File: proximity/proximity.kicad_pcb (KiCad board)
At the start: 2 copper layers, 40 x 30 mm, 32 parts, among them IC1 NRF51822, P1 CONN_3X2, P2 ST-0503, P3 AIN_0_3, P4 AIN_4_7, Q1 MOSFET_N, SW1 SWITCH-4, SW2 SWITCH-4, U1 ANTENNA-NC, X1 FOX924

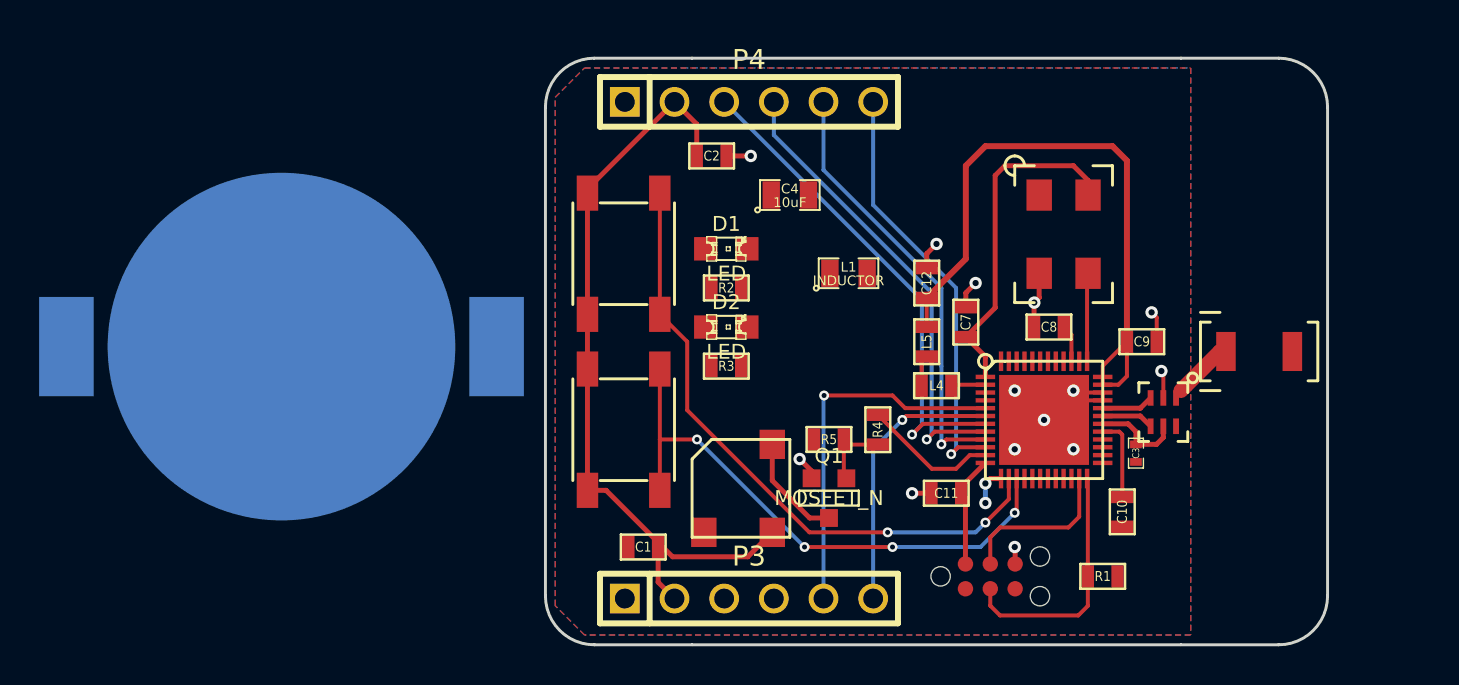
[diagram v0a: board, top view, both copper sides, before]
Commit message: Proximity tag routing done
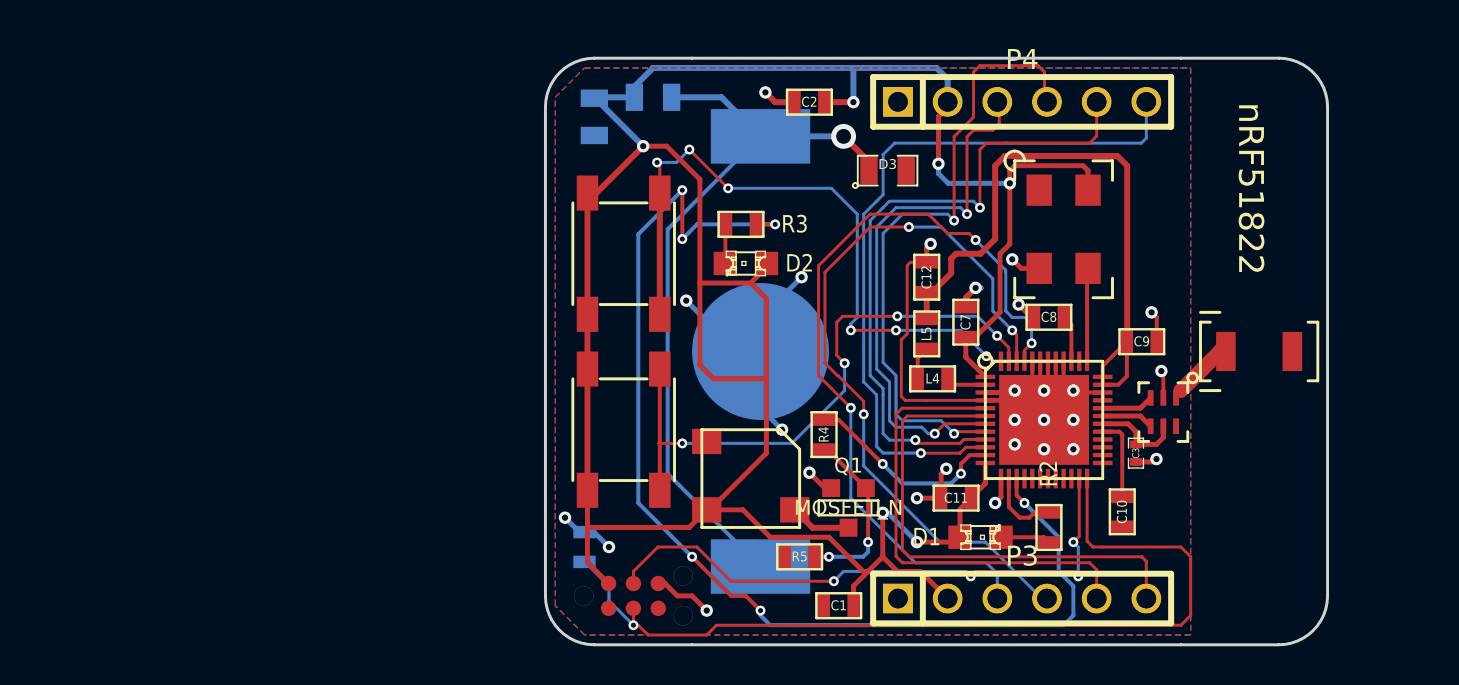
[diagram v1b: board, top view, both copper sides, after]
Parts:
- added D3: DIODE, SM0805, F.Cu at (112.5, 105.8)
- C4, L1, R1: moved to B.Cu
- moved R1 26.5 mm to (97.0, 125.0), turned to 90 degrees
- moved BT1 24.5 mm to (106.0, 115.0), turned to 90 degrees
- moved R2 20.6 mm to (120.8, 124.0), turned to 90 degrees
- moved D1 19.7 mm to (117.2, 124.5)
- moved P1 18.3 mm to (99.5, 127.5)
- moved P3 14.0 mm to (119.4, 127.6)
- moved P4 14.0 mm to (119.4, 102.2)
- moved L1 13.5 mm to (100.5, 102.0), turned to 180 degrees
- moved C4 10.8 mm to (97.5, 103.0), turned to 270 degrees
- moved C1 10.4 mm to (110.0, 128.0)
- moved R3 7.29 mm to (105.0, 108.5)
- moved R5 6.18 mm to (108.0, 125.5)
- moved C2 5.71 mm to (108.5, 102.2), turned to 0 degrees
- moved D2 3.40 mm to (105.2, 110.5), turned to 180 degrees
- moved R4 2.76 mm to (109.2, 119.2)
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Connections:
- IC1 pad 14: /SW1 -> /LED1
- IC1 pad 15: /SW2 -> /LED2
- IC1 pad 3: (no net) -> GND
- IC1 pad 4: (no net) -> GND
- IC1 pad 40: (no net) -> GND
- IC1 pad 41: (no net) -> GND
- IC1 pad 42: (no net) -> GND
- IC1 pad 43: (no net) -> GND
- IC1 pad 44: (no net) -> GND
- IC1 pad 47: (no net) -> /SW2
- IC1 pad 48: (no net) -> /SW1
- R2 pad 2: (no net) -> /LED1
- R3 pad 2: (no net) -> /LED2
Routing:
- net VCC: track 62.6 -> 145.2 mm, vias 0 -> 6
- net /LED2: track 0.00 -> 58.9 mm, vias 0 -> 6
- net GND: track 34.8 -> 86.4 mm, vias 16 -> 27
- net /AIN0: track 0.00 -> 40.5 mm, vias 0 -> 3
- net /AIN1: track 0.00 -> 38.3 mm, vias 0 -> 3
- net N-000003: track 0.00 -> 37.8 mm, vias 0 -> 1
- net /SWCLK: track 12.8 -> 46.1 mm, vias 0 -> 1
- net /SWDIO: track 8.30 -> 30.5 mm, vias 0 -> 4
- net /AIN7: track 21.8 -> 37.1 mm
- net /AIN6: track 22.4 -> 33.9 mm, vias 1 -> 2
- net /AIN3: track 14.1 -> 25.6 mm, vias 1 -> 0
- net /AIN5: track 23.9 -> 32.2 mm, vias 1 -> 2
- net N-0000029: track 3.88 -> 9.16 mm, vias 0 -> 2
- net /AIN2: track 18.9 -> 24.0 mm, vias 1 -> 0
- net /LED1: track 0.00 -> 3.84 mm
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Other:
- net class logic added: clearance 0.1524, trace_width 0.1524, via_dia 0.508, via_drill 0.381
- board text added: "Guan Yang 2013"
- board text added: "nRF51822"

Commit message: Minor changes
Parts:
- added D4: DIODE, SM0805, F.Cu at (107.8, 113.5)
- IC1: footprint QFN48+1-0.4MM -> QFN48+1-0.4MM-SHORTPADS
- moved R5 8.43 mm to (106.2, 117.2)
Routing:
- net N-0000024: track 3.13 -> 11.8 mm
- net GND: track 86.4 -> 94.2 mm, vias 27 -> 28
- net VCC: track 145.2 -> 139.0 mm
- net N-0000030: track 9.16 -> 9.74 mm
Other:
- board text added: "01A2"
- board text added: "02A3"
- board text added: "03A4"
- board text added: "04A5"
- board text added: "05A6"
- board text added: "06A7"
- board text added: "26A0"
- board text added: "27A1"
- board text added: "3V3"
- board text added: "GND"

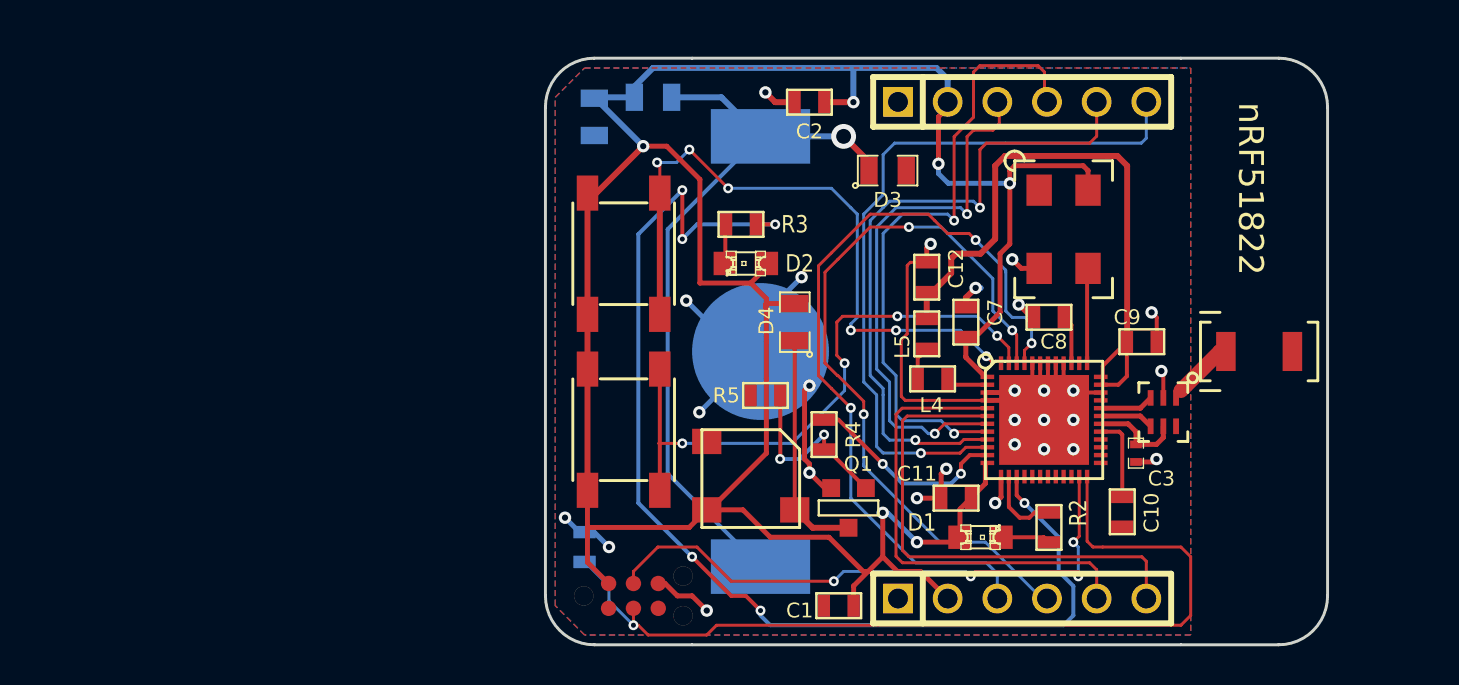
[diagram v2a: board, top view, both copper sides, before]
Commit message: nRF51822 proximity tag updates: - Ordinary crystal instead of CMOS oscillator - Regular pin header for SWDIO and SWCLK
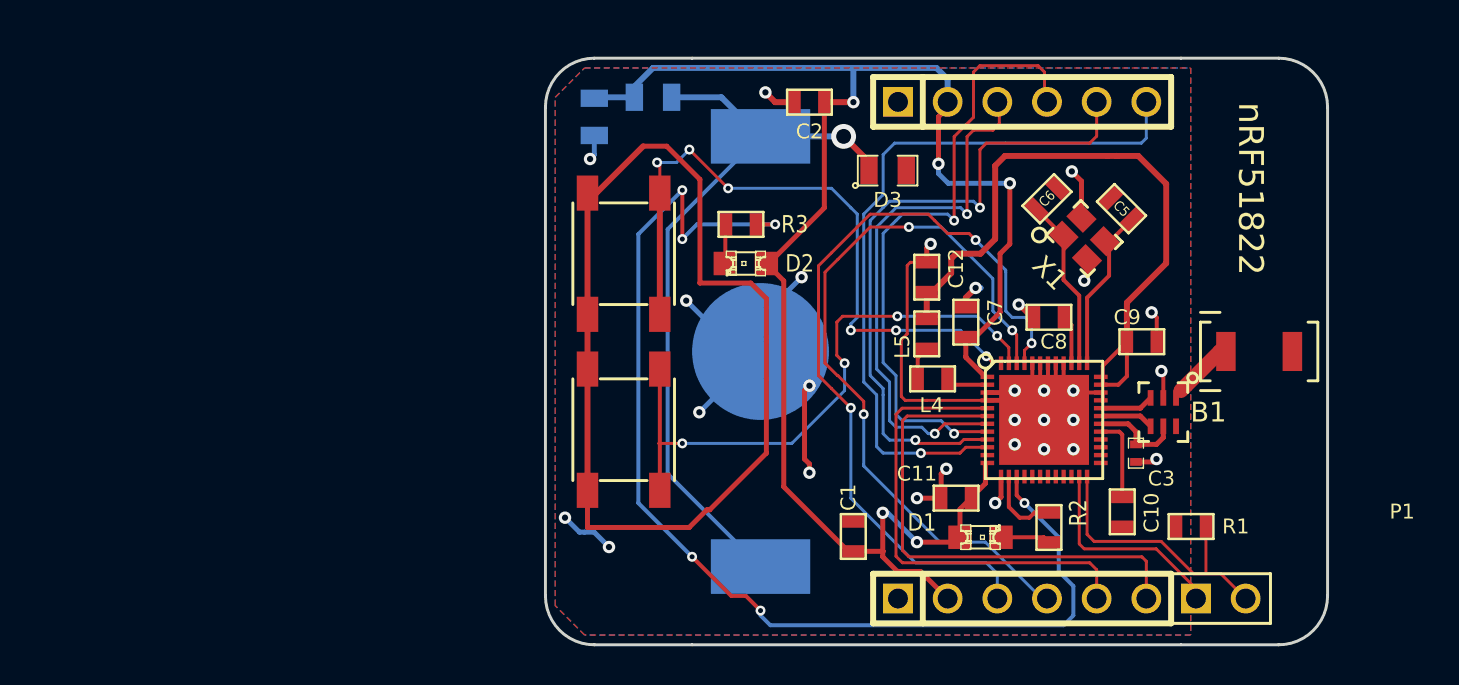
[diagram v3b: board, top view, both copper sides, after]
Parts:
- removed D4: DIODE, SM0805
- removed P2: ST-0503, BUZZER-ST-5MM
- removed Q1: MOSFET_N, SOT23GDS
- removed R4: 100R, SM0603
- removed R5: 10K, SM0603
- added C5: 12pF, SM0603, F.Cu at (124.5, 107.7)
- added C6: 12pF, SM0603, F.Cu at (120.7, 107.2)
- P1: value CONN_3X2 -> CONN_2; footprint TC2030-MCP-NL -> PIN_ARRAY_2X1
- R1: moved to F.Cu
- X1: value FOX924 -> NX2520SA; footprint OSCILLATOR-FOX924 -> CRYSTAL-2520
- moved R1 31.0 mm to (128.0, 124.0), turned to 180 degrees
- moved P1 30.0 mm to (129.5, 127.6)
- moved C1 3.62 mm to (110.7, 124.5), turned to 270 degrees
- moved X1 1.15 mm to (122.6, 109.2), turned to 315 degrees
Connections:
- IC1 pad 11: /BUZZER -> (no net)
- IC1 pad 38: (no net) -> N-0000026
- P1 pad 1: (no net) -> /SWDIO
- P1 pad 2: VCC -> /SWCLK
- SW1 pad 1: VCC -> GND
- SW1 pad 2: VCC -> GND
- SW2 pad 1: VCC -> GND
- SW2 pad 2: VCC -> GND
- X1 pad 1: (no net) -> N-0000026
- X1 pad 4: VCC -> GND
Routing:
- net VCC: track 139.0 -> 86.2 mm, vias 6 -> 5
- net GND: track 94.2 -> 142.5 mm, vias 28 -> 27
- net /SWCLK: track 46.1 -> 15.0 mm, vias 1 -> 0
- net /SWDIO: track 30.5 -> 10.9 mm, vias 4 -> 0
- net N-0000024: track 11.8 -> 0.00 mm
- net /BUZZER: track 10.5 -> 0.00 mm, vias 2 -> 0
- net N-0000030: track 9.74 -> 0.00 mm, vias 2 -> 0
- net N-0000026: track 0.00 -> 8.80 mm
- net N-0000023: track 4.77 -> 8.64 mm
- net (no net): track 0.00 -> 2.87 mm, vias 0 -> 2
- net AVDD: track 32.8 -> 35.1 mm
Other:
- board text added: "SWCLK"
- board text added: "SWDIO"

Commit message: proximity board updates
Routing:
- net (no net): track 2.87 -> 0.00 mm, vias 2 -> 0
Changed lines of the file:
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@@
     (thickness 1.6)
     (drawings 28)
-    (tracks 494)
+    (tracks 488)
     (zones 0)
     (modules 31)
@@
   (gr_line (start 127.5 130) (end 102.5 130) (angle 90) (layer Edge.Cuts) (width 0.15))
   (gr_line (start 102.5 100) (end 127.5 100) (angle 90) (layer Edge.Cuts) (width 0.15))
-  (segment (start 97 124.238) (end 96.738 124.238) (width 0.254) (layer B.Cu) (net 0))
-  (via (at 96 123.5) (size 0.635) (layers F.Cu B.Cu) (net 0))
-  (segment (start 96.738 124.238) (end 96 123.5) (width 0.254) (layer B.Cu) (net 0))
-  (segment (start 97 124.238) (end 97.488 124.238) (width 0.254) (layer B.Cu) (net 0))
-  (via (at 98.25 125) (size 0.635) (layers F.Cu B.Cu) (net 0))
-  (segment (start 97.488 124.238) (end 98.25 125) (width 0.254) (layer B.Cu) (net 0))
   (segment (start 116.5606 108.966) (end 116.666 108.966) (width 0.1524) (layer F.Cu) (net 1))
   (segment (start 108.966 110.617) (end 108.966 116.2304) (width 0.1524) (layer F.Cu) (net 1))
@@
   (segment (start 123.5 115.738) (end 124.738 114.5) (width 0.2032) (layer F.Cu) (net 18))
   (segment (start 123.5 116.7) (end 123.5 116.3) (width 0.2032) (layer F.Cu) (net 18))
+  (segment (start 97.15 124) (end 102.35 124) (width 0.254) (layer F.Cu) (net 19))
+  (segment (start 102.9 106.2) (end 102.9 111.5) (width 0.254) (layer F.Cu) (net 19))
+  (segment (start 102.9 111.5) (end 105.5 111.5) (width 0.254) (layer F.Cu) (net 19))
+  (segment (start 106.29902 112.29902) (end 105.5 111.5) (width 0.254) (layer F.Cu) (net 19))
+  (segment (start 106.29902 116.4) (end 106.29902 114.5) (width 0.254) (layer F.Cu) (net 19))
+  (segment (start 106.29902 112.75) (end 106.29902 112.29902) (width 0.254) (layer F.Cu) (net 19))
+  (segment (start 106.29902 114.25) (end 106.29902 112.75) (width 0.254) (layer F.Cu) (net 19))
+  (segment (start 106.29902 114.5) (end 106.29902 114.25) (width 0.254) (layer F.Cu) (net 19))
+  (segment (start 106.29902 120.20098) (end 106.29902 116.4) (width 0.254) (layer F.Cu) (net 19))
+  (segment (start 102.35 124) (end 103.25 123.1) (width 0.254) (layer F.Cu) (net 19))
+  (segment (start 103.4 123.1) (end 106.29902 120.20098) (width 0.254) (layer F.Cu) (net 19))
+  (segment (start 103.25 123.1) (end 103.4 123.1) (width 0.254) (layer F.Cu) (net 19))
+  (segment (start 97.15 122.1) (end 97.15 124) (width 0.254) (layer F.Cu) (net 19))
+  (segment (start 97.6 106.9) (end 97.15 106.9) (width 0.3048) (layer F.Cu) (net 19))
+  (segment (start 100 104.5) (end 97.6 106.9) (width 0.3048) (layer F.Cu) (net 19))
+  (segment (start 101.2 104.5) (end 102.9 106.2) (width 0.254) (layer F.Cu) (net 19))
+  (segment (start 100 104.5) (end 101.2 104.5) (width 0.254) (layer F.Cu) (net 19))
   (segment (start 97.5 103.9525) (end 97.5 104.938) (width 0.254) (layer B.Cu) (net 19))
   (via (at 97.282 105.156) (size 0.635) (layers F.Cu B.Cu) (net 19))
@@
   (via (at 122 120) (size 0.635) (layers F.Cu B.Cu) (net 19))
   (via (at 122 117) (size 0.635) (layers F.Cu B.Cu) (net 19))
-  (segment (start 97.15 124) (end 102.35 124) (width 0.254) (layer F.Cu) (net 19))
-  (segment (start 100 104.5) (end 101.2 104.5) (width 0.254) (layer F.Cu) (net 19))
-  (segment (start 101.2 104.5) (end 102.9 106.2) (width 0.254) (layer F.Cu) (net 19))
-  (segment (start 100 104.5) (end 97.6 106.9) (width 0.3048) (layer F.Cu) (net 19))
-  (segment (start 97.6 106.9) (end 97.15 106.9) (width 0.3048) (layer F.Cu) (net 19))
-  (segment (start 97.15 122.1) (end 97.15 124) (width 0.254) (layer F.Cu) (net 19))
   (segment (start 97.15 115.9) (end 97.15 122.1) (width 0.3048) (layer F.Cu) (net 19))
   (segment (start 97.15 113.1) (end 97.15 115.9) (width 0.3048) (layer F.Cu) (net 19))
   (segment (start 97.15 106.9) (end 97.15 113.1) (width 0.3048) (layer F.Cu) (net 19))
-  (segment (start 103.25 123.1) (end 103.4 123.1) (width 0.254) (layer F.Cu) (net 19))
-  (segment (start 103.4 123.1) (end 106.29902 120.20098) (width 0.254) (layer F.Cu) (net 19))
-  (segment (start 102.35 124) (end 103.25 123.1) (width 0.254) (layer F.Cu) (net 19))
-  (segment (start 106.29902 120.20098) (end 106.29902 116.4) (width 0.254) (layer F.Cu) (net 19))
-  (segment (start 106.29902 114.5) (end 106.29902 114.25) (width 0.254) (layer F.Cu) (net 19))
-  (segment (start 106.29902 114.25) (end 106.29902 112.75) (width 0.254) (layer F.Cu) (net 19))
-  (segment (start 106.29902 112.75) (end 106.29902 112.29902) (width 0.254) (layer F.Cu) (net 19))
-  (segment (start 106.29902 116.4) (end 106.29902 114.5) (width 0.254) (layer F.Cu) (net 19))
-  (segment (start 106.29902 112.29902) (end 105.5 111.5) (width 0.254) (layer F.Cu) (net 19))
-  (segment (start 102.9 111.5) (end 105.5 111.5) (width 0.254) (layer F.Cu) (net 19))
-  (segment (start 102.9 106.2) (end 102.9 111.5) (width 0.254) (layer F.Cu) (net 19))
   (segment (start 127.25024 117.3761) (end 127.25024 117.24976) (width 0.2032) (layer F.Cu) (net 20))
   (segment (start 129.5 115) (end 127.5 117) (width 0.762) (layer F.Cu) (net 20))
